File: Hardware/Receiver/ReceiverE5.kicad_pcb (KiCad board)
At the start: 2 copper layers, 50 x 30 mm, 41 parts, among them J1 KBUS, J2 AVR-PDI-6A, J3 CONN_01X08, J4 CONN_01X06, J5 CONN_01X06, J6 CONN_01X04, J7 CONN_01X04, U1 ATXMEGA32E5-A, U2 LM2731, U3 SN74LV07A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

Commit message: Boost/linear reg
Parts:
- moved J2 30.0 mm to (108.5, 97.7)
- moved C9 23.8 mm to (103.5, 81.0), turned to 0 degrees
- moved U5 17.3 mm to (103.5, 84.3), turned to 90 degrees
- moved R5 6.90 mm to (94.0, 81.2), turned to 180 degrees
- moved C6 0.10 mm to (97.6, 81.2)
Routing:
- net +5V: track 0.00 -> 17.6 mm
- net Net-(C6-Pad2): track 0.00 -> 6.34 mm
- net Net-(D2-Pad2): track 0.00 -> 5.95 mm
- net /BOOST_IN: track 0.00 -> 5.75 mm
- net +3V3: track 0.00 -> 2.28 mm
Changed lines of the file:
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@@
     (thickness 1.6)
     (drawings 11)
-    (tracks 369)
+    (tracks 396)
     (zones 0)
     (modules 41)
@@
   )
   (setup
-    (last_trace_width 0.15)
+    (last_trace_width 0.75)
     (user_trace_width 0.15)
     (user_trace_width 0.2)
     (user_trace_width 0.3)
+    (user_trace_width 0.5)
+    (user_trace_width 0.75)
     (trace_clearance 0.1016)
     (zone_clearance 0.508)
@@
   )
   (module Capacitors_SMD:C_0603 (layer F.Cu)
-    (at 97.6 81.3 180)
+    (at 97.6 81.2 180)
     (descr "Capacitor SMD 0603, reflow soldering, AVX (see smccp.pdf)")
     (tags "capacitor 0603")
@@
   )
   (module Capacitors_SMD:C_0603 (layer F.Cu)
-    (at 104.9 104.8 180)
+    (at 103.5 81)
     (descr "Capacitor SMD 0603, reflow soldering, AVX (see smccp.pdf)")
     (tags "capacitor 0603")
     (attr smd)
-    (fp_text reference C9 (at 0 -1.9 180) (layer F.SilkS)
-      (effects (font (size 1 1) (thickness 0.15)))
-    )
-    (fp_text value 10u (at 0 1.9 180) (layer F.Fab)
+    (fp_text reference C9 (at 0 -1.9) (layer F.SilkS)
+      (effects (font (size 1 1) (thickness 0.15)))
+    )
+    (fp_text value 10u (at 0 1.9) (layer F.Fab)
       (effects (font (size 1 1) (thickness 0.15)))
     )
@@
     (fp_line (start -0.35 -0.6) (end 0.35 -0.6) (layer F.SilkS) (width 0.15))
     (fp_line (start 0.35 0.6) (end -0.35 0.6) (layer F.SilkS) (width 0.15))
-    (pad 1 smd rect (at -0.75 0 180) (size 0.8 0.75) (layers F.Cu F.Paste F.Mask)
+    (pad 1 smd rect (at -0.75 0) (size 0.8 0.75) (layers F.Cu F.Paste F.Mask)
       (net 5 +3V3))
-    (pad 2 smd rect (at 0.75 0 180) (size 0.8 0.75) (layers F.Cu F.Paste F.Mask)
+    (pad 2 smd rect (at 0.75 0) (size 0.8 0.75) (layers F.Cu F.Paste F.Mask)
       (net 2 GND))
     (model Capacitors_SMD.3dshapes/C_0603.wrl
@@
   )
   (module Pin_Headers:Pin_Header_Straight_2x03 (layer F.Cu)
-    (at 78.74 100.9 270)
+    (at 108.54 97.7 270)
     (descr "Through hole pin header")
     (tags "pin header")
@@
   )
   (module Resistors_SMD:R_0603 (layer F.Cu)
-    (at 100.6 83.2)
+    (at 94 81.2 180)
     (descr "Resistor SMD 0603, reflow soldering, Vishay (see dcrcw.pdf)")
     (tags "resistor 0603")
     (attr smd)
-    (fp_text reference R5 (at 0 -1.9) (layer F.SilkS)
-      (effects (font (size 1 1) (thickness 0.15)))
-    )
-    (fp_text value 15k (at 0 1.9) (layer F.Fab)
+    (fp_text reference R5 (at 0 -1.9 180) (layer F.SilkS)
+      (effects (font (size 1 1) (thickness 0.15)))
+    )
+    (fp_text value 15k (at 0 1.9 180) (layer F.Fab)
       (effects (font (size 1 1) (thickness 0.15)))
     )
@@
     (fp_line (start 0.5 0.675) (end -0.5 0.675) (layer F.SilkS) (width 0.15))
     (fp_line (start -0.5 -0.675) (end 0.5 -0.675) (layer F.SilkS) (width 0.15))
-    (pad 1 smd rect (at -0.75 0) (size 0.5 0.9) (layers F.Cu F.Paste F.Mask)
+    (pad 1 smd rect (at -0.75 0 180) (size 0.5 0.9) (layers F.Cu F.Paste F.Mask)
       (net 7 "Net-(C6-Pad2)"))
-    (pad 2 smd rect (at 0.75 0) (size 0.5 0.9) (layers F.Cu F.Paste F.Mask)
+    (pad 2 smd rect (at 0.75 0 180) (size 0.5 0.9) (layers F.Cu F.Paste F.Mask)
       (net 2 GND))
     (model Resistors_SMD.3dshapes/R_0603.wrl
@@
   )
   (module TO_SOT_Packages_SMD:SOT-23-5 (layer F.Cu)
-    (at 104.9 101.5 270)
+    (at 103.5 84.3 90)
     (descr "5-pin SOT23 package")
     (tags SOT-23-5)
     (attr smd)
-    (fp_text reference U5 (at -0.05 -2.55 270) (layer F.SilkS)
-      (effects (font (size 1 1) (thickness 0.15)))
-    )
-    (fp_text value TPS78233 (at -0.05 2.35 270) (layer F.Fab)
+    (fp_text reference U5 (at -0.05 -2.55 90) (layer F.SilkS)
+      (effects (font (size 1 1) (thickness 0.15)))
+    )
+    (fp_text value TPS78233 (at -0.05 2.35 90) (layer F.Fab)
       (effects (font (size 1 1) (thickness 0.15)))
     )
@@
     (fp_line (start -0.25 1.45) (end 0.25 1.45) (layer F.SilkS) (width 0.15))
     (fp_line (start -0.25 -1.45) (end -0.25 1.45) (layer F.SilkS) (width 0.15))
-    (pad 1 smd rect (at -1.1 -0.95 270) (size 1.06 0.65) (layers F.Cu F.Paste F.Mask)
+    (pad 1 smd rect (at -1.1 -0.95 90) (size 1.06 0.65) (layers F.Cu F.Paste F.Mask)
       (net 6 +5V))
-    (pad 2 smd rect (at -1.1 0 270) (size 1.06 0.65) (layers F.Cu F.Paste F.Mask)
-      (net 2 GND))
-    (pad 3 smd rect (at -1.1 0.95 270) (size 1.06 0.65) (layers F.Cu F.Paste F.Mask)
+    (pad 2 smd rect (at -1.1 0 90) (size 1.06 0.65) (layers F.Cu F.Paste F.Mask)
+      (net 2 GND))
+    (pad 3 smd rect (at -1.1 0.95 90) (size 1.06 0.65) (layers F.Cu F.Paste F.Mask)
       (net 6 +5V))
-    (pad 4 smd rect (at 1.1 0.95 270) (size 1.06 0.65) (layers F.Cu F.Paste F.Mask)
-      (net 2 GND))
-    (pad 5 smd rect (at 1.1 -0.95 270) (size 1.06 0.65) (layers F.Cu F.Paste F.Mask)
+    (pad 4 smd rect (at 1.1 0.95 90) (size 1.06 0.65) (layers F.Cu F.Paste F.Mask)
+      (net 2 GND))
+    (pad 5 smd rect (at 1.1 -0.95 90) (size 1.06 0.65) (layers F.Cu F.Paste F.Mask)
       (net 5 +3V3))
     (model TO_SOT_Packages_SMD.3dshapes/SOT-23-5.wrl
@@
     (arrow2b (pts (xy 117 61) (xy 115.873496 61.586421)))
   )
+  (segment (start 92.6 85.55) (end 92.6 89.05) (width 0.75) (layer F.Cu) (net 4))
+  (segment (start 92.6 89.05) (end 92.35 89.3) (width 0.75) (layer F.Cu) (net 4))
+  (segment (start 92.6 83.65) (end 92.6 85.55) (width 0.75) (layer F.Cu) (net 4))
+  (segment (start 102.55 83.2) (end 102.55 81.2) (width 0.75) (layer F.Cu) (net 5))
+  (segment (start 102.55 81.2) (end 102.75 81) (width 0.75) (layer F.Cu) (net 5))
+  (segment (start 104.23 86.9) (end 102.5 86.9) (width 0.75) (layer F.Cu) (net 6))
+  (segment (start 102.5 86.9) (end 100.135 86.9) (width 0.75) (layer F.Cu) (net 6))
+  (segment (start 102.55 85.4) (end 102.55 86.85) (width 0.75) (layer F.Cu) (net 6))
+  (segment (start 102.55 86.85) (end 102.5 86.9) (width 0.75) (layer F.Cu) (net 6))
+  (segment (start 100.135 85.4) (end 100.135 86.9) (width 0.75) (layer F.Cu) (net 6))
+  (segment (start 100.135 86.9) (end 100.135 88.185) (width 0.75) (layer F.Cu) (net 6))
+  (segment (start 104.45 85.4) (end 104.45 86.68) (width 0.75) (layer F.Cu) (net 6))
+  (segment (start 104.45 86.68) (end 104.23 86.9) (width 0.75) (layer F.Cu) (net 6))
+  (segment (start 98.35 83.2) (end 98.35 81.2) (width 0.3) (layer F.Cu) (net 6))
+  (segment (start 98.35 83.2) (end 98.35 83.615) (width 0.3) (layer F.Cu) (net 6))
+  (segment (start 98.35 83.615) (end 100.135 85.4) (width 0.3) (layer F.Cu) (net 6))
+  (segment (start 100.1 90.8) (end 100.1 88.25) (width 0.75) (layer F.Cu) (net 6))
+  (segment (start 100.1 88.25) (end 100.15 88.2) (width 0.75) (layer F.Cu) (net 6))
+  (segment (start 100.135 88.185) (end 100.15 88.2) (width 0.75) (layer F.Cu) (net 6))
+  (segment (start 96.85 81.2) (end 94.75 81.2) (width 0.3) (layer F.Cu) (net 7))
+  (segment (start 96.85 83.2) (end 96.85 81.2) (width 0.3) (layer F.Cu) (net 7))
+  (segment (start 94.8 83.65) (end 96.4 83.65) (width 0.3) (layer F.Cu) (net 7))
+  (segment (start 96.4 83.65) (end 96.85 83.2) (width 0.3) (layer F.Cu) (net 7))
+  (segment (start 94.8 85.55) (end 96.715 85.55) (width 0.75) (layer F.Cu) (net 10))
+  (segment (start 96.715 85.55) (end 96.865 85.4) (width 0.75) (layer F.Cu) (net 10))
+  (segment (start 94.8 85.55) (end 94.8 89.12) (width 0.75) (layer F.Cu) (net 10))
+  (segment (start 94.8 89.12) (end 94.98 89.3) (width 0.75) (layer F.Cu) (net 10))
   (segment (start 84.7 74.9) (end 83.8 74.9) (width 0.2) (layer F.Cu) (net 15))
   (segment (start 84.7 79.35482) (end 84.7 74.9) (width 0.2) (layer B.Cu) (net 15))

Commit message: 2 layer power routing try 1
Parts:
- C5: moved to B.Cu
- moved J2 9.11 mm to (108.1, 88.6)
- moved C10 2.90 mm to (83.7, 65.1), turned to 180 degrees
- moved C5 1.80 mm to (91.2, 65.7)
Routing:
- net /DIR: track 0.00 -> 34.8 mm, vias 0 -> 2
- net +3V3: track 2.28 -> 28.8 mm, vias 0 -> 2
- net Net-(C2-Pad1): track 0.00 -> 8.61 mm
- net Net-(C1-Pad1): track 0.00 -> 7.91 mm
- net /A7: track 21.7 -> 22.7 mm

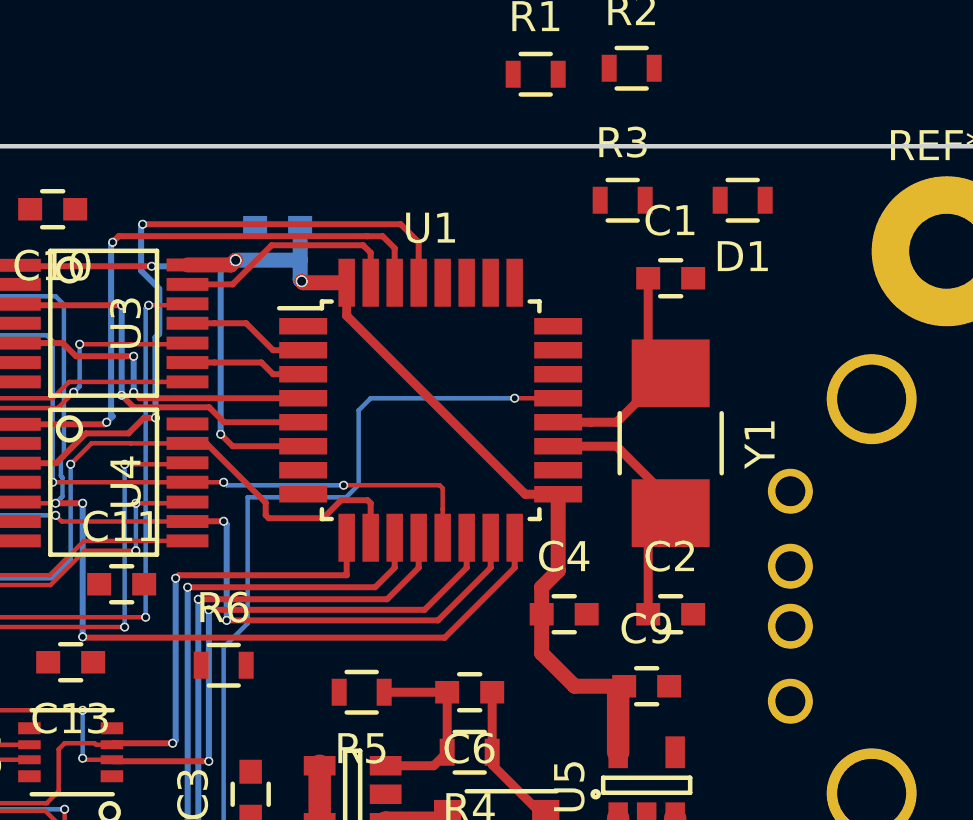
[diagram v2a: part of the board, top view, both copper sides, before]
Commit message: Added missing series termination resistors for KBUS
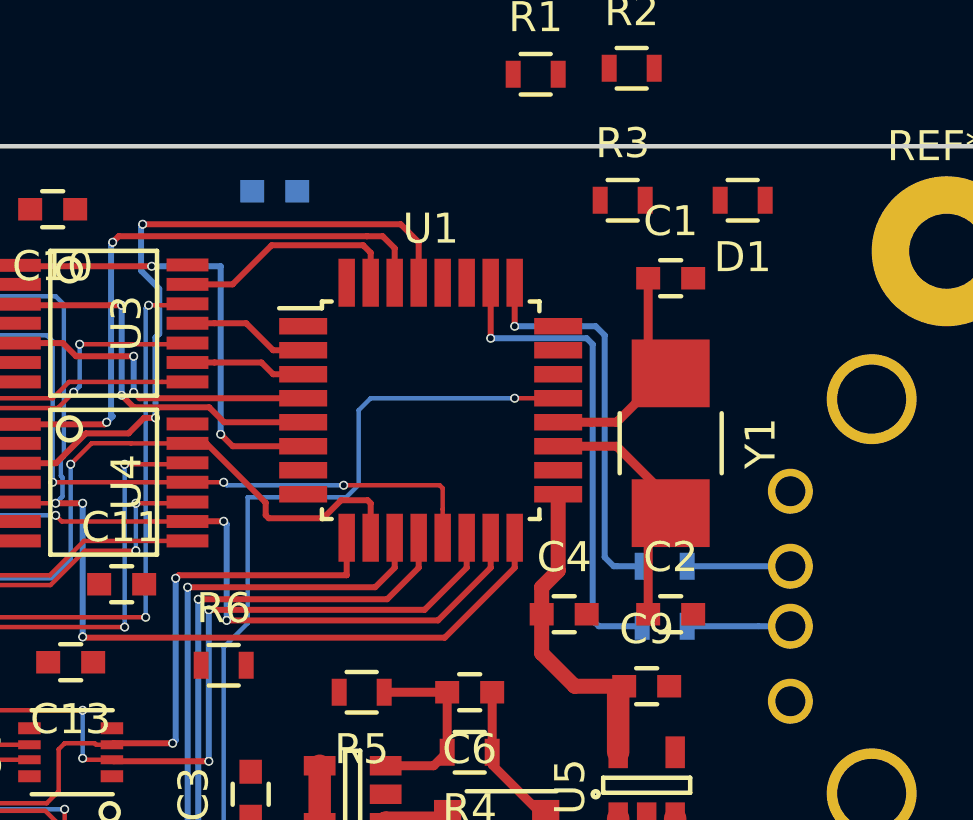
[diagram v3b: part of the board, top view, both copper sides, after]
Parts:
- added R7: 33, Resistors_SMD:R_0603, B.Cu at (104.1, 77.0)
- added R8: 33, Resistors_SMD:R_0603, B.Cu at (104.1, 79.0)
- moved C5 1.20 mm to (91.1, 64.5)
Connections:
- J1 pad 2: /KBUS_TX -> Net-(J1-Pad2)
- J1 pad 3: /KBUS_RX -> Net-(J1-Pad3)
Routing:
- net +3V3: track 28.8 -> 11.0 mm, vias 2 -> 0
- net /KBUS_RX: track 0.00 -> 16.3 mm, vias 0 -> 1
- net /KBUS_TX: track 0.00 -> 13.3 mm, vias 0 -> 1
- net Net-(J1-Pad3): track 0.00 -> 3.44 mm
- net Net-(J1-Pad2): track 0.00 -> 3.44 mm
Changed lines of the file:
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@@
 (kicad_pcb (version 4) (host pcbnew 4.0.2-stable)
   (general
-    (links 0)
-    (no_connects 119)
-    (area 0 0 0 0)
+    (links 121)
+    (no_connects 60)
+    (area 66.924999 62.924999 117.075001 93.075001)
     (thickness 1.6)
     (drawings 11)
-    (tracks 447)
+    (tracks 453)
     (zones 0)
-    (modules 41)
-    (nets 51)
+    (modules 43)
+    (nets 53)
   )
   (page A4)
@@
   )
   (setup
-    (last_trace_width 0.5)
+    (last_trace_width 0.2)
     (user_trace_width 0.15)
     (user_trace_width 0.2)
@@
   (net 49 /A6)
   (net 50 /A5)
+  (net 51 "Net-(J1-Pad3)")
+  (net 52 "Net-(J1-Pad2)")
   (net_class Default "This is the default net class."
     (clearance 0.1016)
@@
     (add_net "Net-(D1-Pad2)")
     (add_net "Net-(D2-Pad2)")
+    (add_net "Net-(J1-Pad2)")
+    (add_net "Net-(J1-Pad3)")
     (add_net "Net-(J2-Pad1)")
     (add_net "Net-(J2-Pad5)")
@@
   )
   (module Capacitors_SMD:C_0603 (layer B.Cu)
-    (at 91.2 65.7 180)
+    (at 91.1 64.5 180)
     (descr "Capacitor SMD 0603, reflow soldering, AVX (see smccp.pdf)")
     (tags "capacitor 0603")
@@
       (net 2 GND))
     (pad 3 thru_hole circle (at 1 2.71) (size 1.50114 1.50114) (drill 1) (layers *.Cu *.Mask)
-      (net 11 /KBUS_RX))
+      (net 51 "Net-(J1-Pad3)"))
     (pad 2 thru_hole circle (at -1 2.71) (size 1.50114 1.50114) (drill 1) (layers *.Cu *.Mask)
-      (net 12 /KBUS_TX))
+      (net 52 "Net-(J1-Pad2)"))
     (pad 1 thru_hole circle (at -3.5 2.71) (size 1.50114 1.50114) (drill 1) (layers *.Cu *.Mask)
       (net 6 +5V))
@@
     (pad 1 thru_hole circle (at 0 0) (size 5 5) (drill 2.5) (layers *.Cu *.Mask))
   )
+  (module Resistors_SMD:R_0603 (layer B.Cu)
+    (at 104.1 77 180)
+    (descr "Resistor SMD 0603, reflow soldering, Vishay (see dcrcw.pdf)")
+    (tags "resistor 0603")
+    (attr smd)
+    (fp_text reference R7 (at 0 1.9 180) (layer B.SilkS)
+      (effects (font (size 1 1) (thickness 0.15)) (justify mirror))
+    )
+    (fp_text value 33 (at 0 -1.9 180) (layer B.Fab)
+      (effects (font (size 1 1) (thickness 0.15)) (justify mirror))
+    )
+    (fp_line (start -1.3 0.8) (end 1.3 0.8) (layer B.CrtYd) (width 0.05))
+    (fp_line (start -1.3 -0.8) (end 1.3 -0.8) (layer B.CrtYd) (width 0.05))
+    (fp_line (start -1.3 0.8) (end -1.3 -0.8) (layer B.CrtYd) (width 0.05))
+    (fp_line (start 1.3 0.8) (end 1.3 -0.8) (layer B.CrtYd) (width 0.05))
+    (fp_line (start 0.5 -0.675) (end -0.5 -0.675) (layer B.SilkS) (width 0.15))
+    (fp_line (start -0.5 0.675) (end 0.5 0.675) (layer B.SilkS) (width 0.15))
+    (pad 1 smd rect (at -0.75 0 180) (size 0.5 0.9) (layers B.Cu B.Paste B.Mask)
+      (net 52 "Net-(J1-Pad2)"))
+    (pad 2 smd rect (at 0.75 0 180) (size 0.5 0.9) (layers B.Cu B.Paste B.Mask)
+      (net 12 /KBUS_TX))
+    (model Resistors_SMD.3dshapes/R_0603.wrl
+      (at (xyz 0 0 0))
+      (scale (xyz 1 1 1))
+      (rotate (xyz 0 0 0))
+    )
+  )
+  (module Resistors_SMD:R_0603 (layer B.Cu)
+    (at 104.1 79 180)
+    (descr "Resistor SMD 0603, reflow soldering, Vishay (see dcrcw.pdf)")
+    (tags "resistor 0603")
+    (attr smd)
+    (fp_text reference R8 (at 0 1.9 180) (layer B.SilkS)
+      (effects (font (size 1 1) (thickness 0.15)) (justify mirror))
+    )
+    (fp_text value 33 (at 0 -1.9 180) (layer B.Fab)
+      (effects (font (size 1 1) (thickness 0.15)) (justify mirror))
+    )
+    (fp_line (start -1.3 0.8) (end 1.3 0.8) (layer B.CrtYd) (width 0.05))
+    (fp_line (start -1.3 -0.8) (end 1.3 -0.8) (layer B.CrtYd) (width 0.05))
+    (fp_line (start -1.3 0.8) (end -1.3 -0.8) (layer B.CrtYd) (width 0.05))
+    (fp_line (start 1.3 0.8) (end 1.3 -0.8) (layer B.CrtYd) (width 0.05))
+    (fp_line (start 0.5 -0.675) (end -0.5 -0.675) (layer B.SilkS) (width 0.15))
+    (fp_line (start -0.5 0.675) (end 0.5 0.675) (layer B.SilkS) (width 0.15))
+    (pad 1 smd rect (at -0.75 0 180) (size 0.5 0.9) (layers B.Cu B.Paste B.Mask)
+      (net 51 "Net-(J1-Pad3)"))
+    (pad 2 smd rect (at 0.75 0 180) (size 0.5 0.9) (layers B.Cu B.Paste B.Mask)
+      (net 11 /KBUS_RX))
+    (model Resistors_SMD.3dshapes/R_0603.wrl
+      (at (xyz 0 0 0))
+      (scale (xyz 1 1 1))
+      (rotate (xyz 0 0 0))
+    )
+  )
   (gr_line (start 67 91) (end 67 65) (layer Edge.Cuts) (width 0.15))
   (gr_line (start 115 93) (end 69 93) (layer Edge.Cuts) (width 0.15))
@@
   (segment (start 92.6 89.05) (end 92.35 89.3) (width 0.75) (layer F.Cu) (net 4))
   (segment (start 92.6 83.65) (end 92.6 85.55) (width 0.75) (layer F.Cu) (net 4))
-  (segment (start 91.95 65.7) (end 91.95 66.8) (width 0.5) (layer B.Cu) (net 5))
-  (segment (start 91.95 66.8) (end 91.95 67.45) (width 0.5) (layer B.Cu) (net 5))
-  (segment (start 89.8 66.8) (end 91.95 66.8) (width 0.5) (layer B.Cu) (net 5))
-  (segment (start 88.194 66.9569) (end 89.6431 66.9569) (width 0.5) (layer F.Cu) (net 5))
-  (segment (start 89.6431 66.9569) (end 89.8 66.8) (width 0.5) (layer F.Cu) (net 5))
-  (via (at 89.8 66.8) (size 0.4) (drill 0.3) (layers F.Cu B.Cu) (net 5))
-  (segment (start 91.95 67.45) (end 92 67.5) (width 0.5) (layer B.Cu) (net 5))
-  (segment (start 93.5 67.55) (end 92.05 67.55) (width 0.5) (layer F.Cu) (net 5))
-  (segment (start 92.05 67.55) (end 92 67.5) (width 0.5) (layer F.Cu) (net 5))
-  (via (at 92 67.5) (size 0.4) (drill 0.3) (layers F.Cu B.Cu) (net 5))
-  (segment (start 93.5 67.55) (end 93.5 68.65) (width 0.3) (layer F.Cu) (net 5))
-  (segment (start 93.5 68.65) (end 99.45 74.6) (width 0.3) (layer F.Cu) (net 5))
-  (segment (start 99.45 74.6) (end 100.55 74.6) (width 0.3) (layer F.Cu) (net 5))
   (segment (start 100 79.9) (end 101.1 81) (width 0.5) (layer F.Cu) (net 5))
   (segment (start 101.1 81) (end 102.75 81) (width 0.5) (layer F.Cu) (net 5))
@@
   (segment (start 94.8 85.55) (end 94.8 89.12) (width 0.75) (layer F.Cu) (net 10))
   (segment (start 94.8 89.12) (end 94.98 89.3) (width 0.75) (layer F.Cu) (net 10))
+  (segment (start 98.3 69.4) (end 98.3 67.55) (width 0.2) (layer F.Cu) (net 11))
+  (segment (start 101.7 69.6) (end 101.5 69.4) (width 0.2) (layer B.Cu) (net 11))
+  (segment (start 101.5 69.4) (end 98.3 69.4) (width 0.2) (layer B.Cu) (net 11))
+  (via (at 98.3 69.4) (size 0.3016) (drill 0.2) (layers F.Cu B.Cu) (net 11))
+  (segment (start 101.7 78.8) (end 101.7 69.6) (width 0.2) (layer B.Cu) (net 11))
+  (segment (start 101.79839 78.89839) (end 101.7 78.8) (width 0.2) (layer B.Cu) (net 11))
+  (segment (start 101.9 79) (end 101.79839 78.89839) (width 0.2) (layer B.Cu) (net 11))
+  (segment (start 103.35 79) (end 101.9 79) (width 0.2) (layer B.Cu) (net 11))
+  (segment (start 99.1 69) (end 99.1 67.55) (width 0.2) (layer F.Cu) (net 12))
+  (segment (start 102.1 69.3) (end 101.8 69) (width 0.2) (layer B.Cu) (net 12))
+  (segment (start 101.8 69) (end 99.1 69) (width 0.2) (layer B.Cu) (net 12))
+  (via (at 99.1 69) (size 0.3016) (drill 0.2) (layers F.Cu B.Cu) (net 12))
+  (segment (start 102.1 76.7) (end 102.1 69.3) (width 0.2) (layer B.Cu) (net 12))
+  (segment (start 102.4 77) (end 102.1 76.7) (width 0.2) (layer B.Cu) (net 12))
+  (segment (start 102.5 77) (end 102.4 77) (width 0.2) (layer B.Cu) (net 12))
+  (segment (start 103.35 77) (end 102.5 77) (width 0.2) (layer B.Cu) (net 12))
   (segment (start 84.7 74.9) (end 83.8 74.9) (width 0.2) (layer F.Cu) (net 15))
   (segment (start 84.7 79.35482) (end 84.7 74.9) (width 0.2) (layer B.Cu) (net 15))
@@
   (segment (start 94.3 67.55) (end 94.3 66.55) (width 0.2) (layer F.Cu) (net 50))
   (segment (start 94.3 66.55) (end 94.05 66.3) (width 0.2) (layer F.Cu) (net 50))
+  (segment (start 108.29 79) (end 107.228534 79) (width 0.2) (layer B.Cu) (net 51))
+  (segment (start 107.228534 79) (end 104.85 79) (width 0.2) (layer B.Cu) (net 51))
+  (segment (start 108.29 77) (end 104.85 77) (width 0.2) (layer B.Cu) (net 52))
 )
